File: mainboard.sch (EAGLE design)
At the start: 136 parts, among them X1 FH12-24S-0.5SH

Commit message: Finished rev 3 schematic and component placement
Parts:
- added C18, C19: (no value), rcl:C-EUC0603
- added LED2: (no value), eagle-ltspice:LED_ESML0603
- added R12: (no value), resistor:R-US_R0402
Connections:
- new net N$60: LED2.A, R12.2
- net +3V3: now also C18.2, R12.1
- net GND: now also C18.1, C19.1, LED2.C
- net VCC/2: now also C19.2
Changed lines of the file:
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@@
 <?xml version="1.0" encoding="utf-8"?>
 <!DOCTYPE eagle SYSTEM "eagle.dtd">
-<eagle version="8.2.1">
+<eagle version="8.3.2">
 <drawing>
 <settings>
 <setting alwaysvectorfont="no"/>
+<setting keepoldvectorfont="yes"/>
 <setting verticaltext="up"/>
 </settings>
@@
 <part name="TP7" library="testpad" library_urn="urn:adsk.eagle:library:385" deviceset="TP" device="TP20SQ"/>
 <part name="TP8" library="testpad" library_urn="urn:adsk.eagle:library:385" deviceset="TP" device="TP20SQ"/>
+<part name="LED2" library="eagle-ltspice" library_urn="urn:adsk.eagle:library:217" deviceset="LED_E" device="SML0603"/>
+<part name="R12" library="resistor" library_urn="urn:adsk.eagle:library:348" deviceset="R-US_" device="R0402"/>
+<part name="GND18" library="supply1" library_urn="urn:adsk.eagle:library:371" deviceset="GND" device=""/>
+<part name="C18" library="rcl" library_urn="urn:adsk.eagle:library:334" deviceset="C-EU" device="C0603"/>
+<part name="C19" library="rcl" library_urn="urn:adsk.eagle:library:334" deviceset="C-EU" device="C0603"/>
 </parts>
 <sheets>
@@
 </plain>
 <instances>
-<instance part="U$1" gate="G$1" x="96.52" y="116.84"/>
-<instance part="GND1" gate="1" x="109.22" y="101.6"/>
-<instance part="+3V1" gate="G$1" x="86.36" y="132.08"/>
+<instance part="U$1" gate="G$1" x="96.52" y="101.6"/>
+<instance part="GND1" gate="1" x="109.22" y="86.36"/>
+<instance part="+3V1" gate="G$1" x="86.36" y="116.84"/>
 <instance part="U$2" gate="G$1" x="137.16" y="91.44"/>
 <instance part="U$3" gate="G$1" x="241.3" y="93.98"/>
@@
 <instance part="TP7" gate="G$1" x="180.34" y="165.1"/>
 <instance part="TP8" gate="G$1" x="180.34" y="157.48" rot="R180"/>
+<instance part="LED2" gate="G$1" x="91.44" y="132.08" rot="R270"/>
+<instance part="R12" gate="G$1" x="101.6" y="132.08" rot="R180"/>
+<instance part="GND18" gate="1" x="86.36" y="124.46"/>
+<instance part="C18" gate="G$1" x="109.22" y="157.48" rot="R180"/>
+<instance part="C19" gate="G$1" x="104.14" y="160.02" rot="R180"/>
 </instances>
 <busses>
@@
 <pinref part="GND1" gate="1" pin="GND"/>
 <pinref part="U$1" gate="G$1" pin="VSSA"/>
-<wire x1="109.22" y1="104.14" x2="109.22" y2="109.22" width="0.1524" layer="91"/>
+<wire x1="109.22" y1="88.9" x2="109.22" y2="93.98" width="0.1524" layer="91"/>
 <pinref part="U$1" gate="G$1" pin="VSS4"/>
-<wire x1="109.22" y1="109.22" x2="109.22" y2="114.3" width="0.1524" layer="91"/>
-<junction x="109.22" y="109.22"/>
+<wire x1="109.22" y1="93.98" x2="109.22" y2="99.06" width="0.1524" layer="91"/>
+<junction x="109.22" y="93.98"/>
 <pinref part="U$1" gate="G$1" pin="VSS3"/>
-<wire x1="109.22" y1="114.3" x2="109.22" y2="116.84" width="0.1524" layer="91"/>
-<junction x="109.22" y="114.3"/>
+<wire x1="109.22" y1="99.06" x2="109.22" y2="101.6" width="0.1524" layer="91"/>
+<junction x="109.22" y="99.06"/>
 <pinref part="U$1" gate="G$1" pin="VSS2"/>
-<wire x1="109.22" y1="116.84" x2="109.22" y2="119.38" width="0.1524" layer="91"/>
-<junction x="109.22" y="116.84"/>
+<wire x1="109.22" y1="101.6" x2="109.22" y2="104.14" width="0.1524" layer="91"/>
+<junction x="109.22" y="101.6"/>
 <pinref part="U$1" gate="G$1" pin="VSS1"/>
-<wire x1="109.22" y1="119.38" x2="109.22" y2="121.92" width="0.1524" layer="91"/>
-<junction x="109.22" y="119.38"/>
+<wire x1="109.22" y1="104.14" x2="109.22" y2="106.68" width="0.1524" layer="91"/>
+<junction x="109.22" y="104.14"/>
 </segment>
 <segment>
@@
 <pinref part="GND8" gate="1" pin="GND"/>
 </segment>
+<segment>
+<pinref part="GND18" gate="1" pin="GND"/>
+<pinref part="LED2" gate="G$1" pin="C"/>
+<wire x1="86.36" y1="127" x2="86.36" y2="132.08" width="0.1524" layer="91"/>
+</segment>
+<segment>
+<pinref part="C19" gate="G$1" pin="1"/>
+<wire x1="104.14" y1="157.48" x2="104.14" y2="152.4" width="0.1524" layer="91"/>
+<wire x1="114.3" y1="152.4" x2="109.22" y2="152.4" width="0.1524" layer="91"/>
+<pinref part="C18" gate="G$1" pin="1"/>
+<wire x1="109.22" y1="152.4" x2="104.14" y2="152.4" width="0.1524" layer="91"/>
+<wire x1="109.22" y1="152.4" x2="109.22" y2="154.94" width="0.1524" layer="91"/>
+<junction x="109.22" y="152.4"/>
+</segment>
 </net>
 <net name="+3V3" class="0">
@@
 <pinref part="U$1" gate="G$1" pin="VBAT"/>
 <pinref part="U$1" gate="G$1" pin="VDD1"/>
-<wire x1="86.36" y1="127" x2="86.36" y2="121.92" width="0.1524" layer="91"/>
+<wire x1="86.36" y1="111.76" x2="86.36" y2="106.68" width="0.1524" layer="91"/>
 <pinref part="U$1" gate="G$1" pin="VDD2"/>
-<wire x1="86.36" y1="121.92" x2="86.36" y2="119.38" width="0.1524" layer="91"/>
-<junction x="86.36" y="121.92"/>
+<wire x1="86.36" y1="106.68" x2="86.36" y2="104.14" width="0.1524" layer="91"/>
+<junction x="86.36" y="106.68"/>
 <pinref part="U$1" gate="G$1" pin="VDD3"/>
-<wire x1="86.36" y1="119.38" x2="86.36" y2="116.84" width="0.1524" layer="91"/>
-<junction x="86.36" y="119.38"/>
+<wire x1="86.36" y1="104.14" x2="86.36" y2="101.6" width="0.1524" layer="91"/>
+<junction x="86.36" y="104.14"/>
 <pinref part="U$1" gate="G$1" pin="VDD4"/>
-<wire x1="86.36" y1="116.84" x2="86.36" y2="114.3" width="0.1524" layer="91"/>
-<junction x="86.36" y="116.84"/>
+<wire x1="86.36" y1="101.6" x2="86.36" y2="99.06" width="0.1524" layer="91"/>
+<junction x="86.36" y="101.6"/>
 <pinref part="U$1" gate="G$1" pin="VDDA"/>
-<wire x1="86.36" y1="114.3" x2="86.36" y2="109.22" width="0.1524" layer="91"/>
-<junction x="86.36" y="114.3"/>
+<wire x1="86.36" y1="99.06" x2="86.36" y2="93.98" width="0.1524" layer="91"/>
+<junction x="86.36" y="99.06"/>
 <pinref part="+3V1" gate="G$1" pin="+3V3"/>
-<wire x1="86.36" y1="127" x2="86.36" y2="129.54" width="0.1524" layer="91"/>
-<junction x="86.36" y="127"/>
+<wire x1="86.36" y1="111.76" x2="86.36" y2="114.3" width="0.1524" layer="91"/>
+<junction x="86.36" y="111.76"/>
 </segment>
 <segment>
@@
 <wire x1="106.68" y1="142.24" x2="109.22" y2="142.24" width="0.1524" layer="91"/>
 <wire x1="109.22" y1="142.24" x2="109.22" y2="144.78" width="0.1524" layer="91"/>
+<pinref part="R12" gate="G$1" pin="1"/>
+<wire x1="106.68" y1="132.08" x2="109.22" y2="132.08" width="0.1524" layer="91"/>
+<wire x1="109.22" y1="132.08" x2="109.22" y2="142.24" width="0.1524" layer="91"/>
+<junction x="109.22" y="142.24"/>
+</segment>
+<segment>
+<pinref part="C18" gate="G$1" pin="2"/>
+<wire x1="114.3" y1="162.56" x2="109.22" y2="162.56" width="0.1524" layer="91"/>
 </segment>
 </net>
@@
 <pinref part="X1" gate="-23" pin="1"/>
 <wire x1="127" y1="106.68" x2="114.3" y2="106.68" width="0.1524" layer="91"/>
+</segment>
+<segment>
+<pinref part="C19" gate="G$1" pin="2"/>
+<wire x1="114.3" y1="165.1" x2="104.14" y2="165.1" width="0.1524" layer="91"/>
 </segment>
 </net>
@@
 </segment>
 </net>
+<net name="N$60" class="0">
+<segment>
+<pinref part="LED2" gate="G$1" pin="A"/>
+<pinref part="R12" gate="G$1" pin="2"/>
+<wire x1="93.98" y1="132.08" x2="96.52" y2="132.08" width="0.1524" layer="91"/>
+</segment>
+</net>
 </nets>
 </sheet>
@@
 </note>
 <note version="8.2" severity="warning">
-Since Version 8.2, Eagle supports online libraries. The ids
+Since Version 8.2, EAGLE supports online libraries. The ids
 of those online libraries will not be understood (or retained)
 with this version.

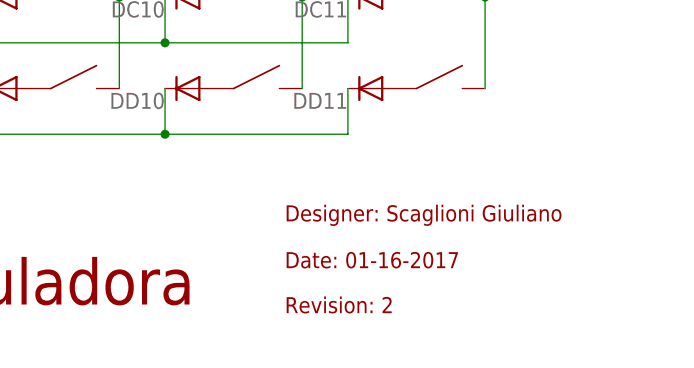
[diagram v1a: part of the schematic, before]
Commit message: Finished Rev 6 pcb routing
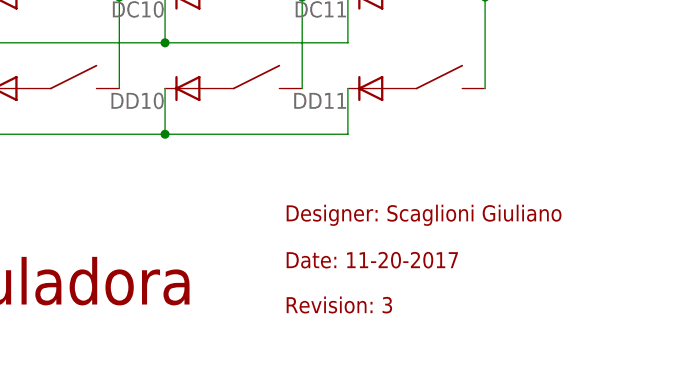
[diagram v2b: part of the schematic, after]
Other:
- note added: "Date: 11-20-2017"
- note added: "Revision: 3"
- note removed: "Date: 01-16-2017"
- note removed: "Revision: 2"
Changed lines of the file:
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@@
 <text x="169.28" y="11.56" size="5.08" layer="94">Calculadora</text>
 <text x="216.5" y="20.8" size="1.778" layer="94">Designer: Scaglioni Giuliano</text>
-<text x="216.5" y="15.6" size="1.778" layer="94">Date: 01-16-2017</text>
-<text x="216.5" y="10.6" size="1.778" layer="94">Revision: 2</text>
+<text x="216.5" y="15.6" size="1.778" layer="94">Date: 11-20-2017</text>
+<text x="216.5" y="10.6" size="1.778" layer="94">Revision: 3</text>
 </plain>
 <instances>
